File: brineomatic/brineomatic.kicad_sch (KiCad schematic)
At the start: 9 parts, among them J21 Conn_01x04_MountingPin

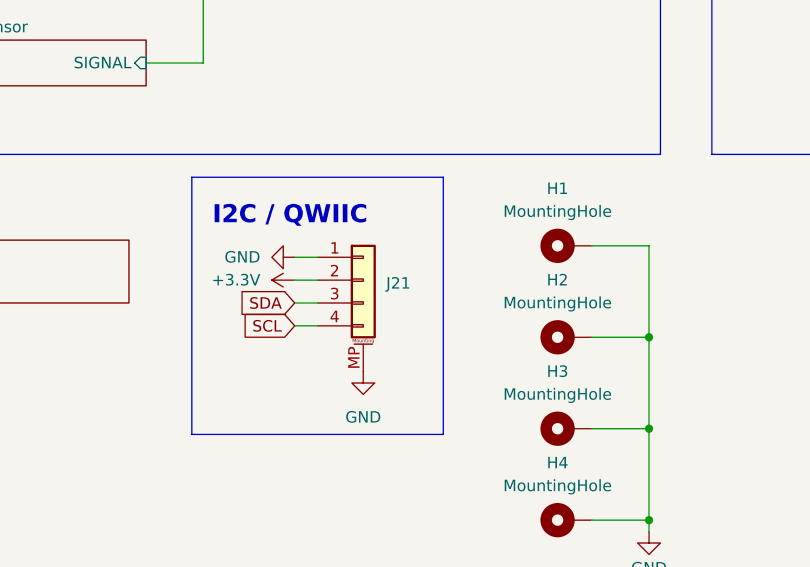
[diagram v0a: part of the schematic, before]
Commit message: added pullup resistor to adc alert
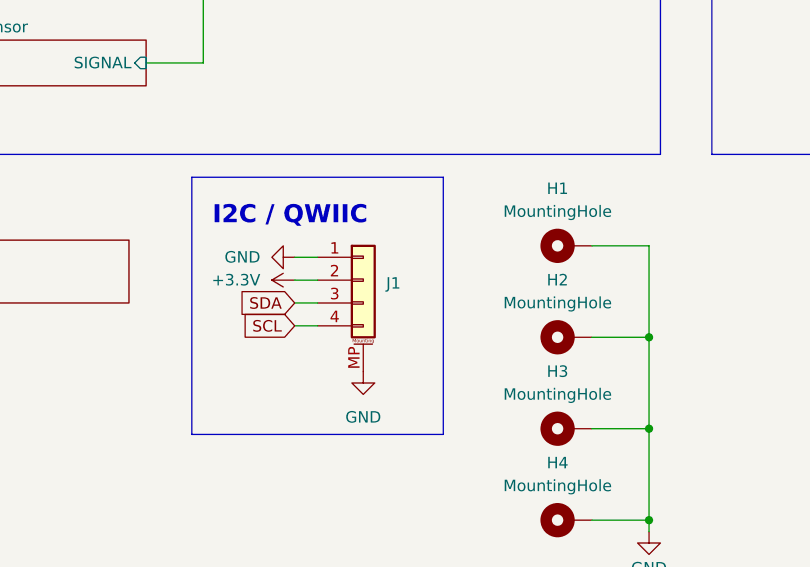
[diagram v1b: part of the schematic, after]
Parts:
- renumbered J21 to J1
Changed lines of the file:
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@@
 		(on_board yes)
 		(dnp no)
-		(property "Reference" "J21"
+		(property "Reference" "J1"
 			(at 92.71 159.1055 0)
 			(effects
@@
 			(project ""
 				(path "/96477ae2-ef08-48f3-8dd4-fe4478541f68"
-					(reference "J21")
+					(reference "J1")
 					(unit 1)
 				)
@@
 		(dnp no)
 		(fields_autoplaced yes)
-		(property "Reference" "#PWR047"
+		(property "Reference" "#PWR03"
 			(at 86.36 158.75 0)
 			(effects
@@
 			(project "brineomatic"
 				(path "/96477ae2-ef08-48f3-8dd4-fe4478541f68"
-					(reference "#PWR047")
+					(reference "#PWR03")
 					(unit 1)
 				)
@@
 		(dnp no)
 		(fields_autoplaced yes)
-		(property "Reference" "#PWR02"
+		(property "Reference" "#PWR01"
 			(at 50.8 63.5 0)
 			(effects
@@
 			(project "brineomatic"
 				(path "/96477ae2-ef08-48f3-8dd4-fe4478541f68"
-					(reference "#PWR02")
+					(reference "#PWR01")
 					(unit 1)
 				)
@@
 		(dnp no)
 		(fields_autoplaced yes)
-		(property "Reference" "#PWR05"
+		(property "Reference" "#PWR07"
 			(at 242.57 95.25 0)
 			(effects
@@
 			(project "brineomatic"
 				(path "/96477ae2-ef08-48f3-8dd4-fe4478541f68"
-					(reference "#PWR05")
+					(reference "#PWR07")
 					(unit 1)
 				)
@@
 		(dnp no)
 		(fields_autoplaced yes)
-		(property "Reference" "#PWR06"
+		(property "Reference" "#PWR08"
 			(at 248.92 73.66 0)
 			(effects
@@
 			(project "brineomatic"
 				(path "/96477ae2-ef08-48f3-8dd4-fe4478541f68"
-					(reference "#PWR06")
+					(reference "#PWR08")
 					(unit 1)
 				)
@@
 		(on_board yes)
 		(dnp no)
-		(property "Reference" "#PWR01"
+		(property "Reference" "#PWR06"
 			(at 121.92 193.04 0)
 			(effects
@@
 			(project "brineomatic"
 				(path "/96477ae2-ef08-48f3-8dd4-fe4478541f68"
-					(reference "#PWR01")
+					(reference "#PWR06")
 					(unit 1)
 				)
@@
 		(dnp no)
 		(fields_autoplaced yes)
-		(property "Reference" "#PWR048"
+		(property "Reference" "#PWR04"
 			(at 90.17 175.26 0)
 			(effects
@@
 			(project "brineomatic"
 				(path "/96477ae2-ef08-48f3-8dd4-fe4478541f68"
-					(reference "#PWR048")
+					(reference "#PWR04")
 					(unit 1)
 				)
@@
 		(dnp no)
 		(fields_autoplaced yes)
-		(property "Reference" "#PWR03"
+		(property "Reference" "#PWR05"
 			(at 104.14 113.03 0)
 			(effects
@@
 			(project ""
 				(path "/96477ae2-ef08-48f3-8dd4-fe4478541f68"
-					(reference "#PWR03")
+					(reference "#PWR05")
 					(unit 1)
 				)
@@
 		(dnp no)
 		(fields_autoplaced yes)
-		(property "Reference" "#PWR04"
+		(property "Reference" "#PWR02"
 			(at 76.2 156.21 0)
 			(effects
@@
 			(project "brineomatic"
 				(path "/96477ae2-ef08-48f3-8dd4-fe4478541f68"
-					(reference "#PWR04")
-					(unit 1)
-				)
+					(reference "#PWR02")
+					(unit 1)
+				)

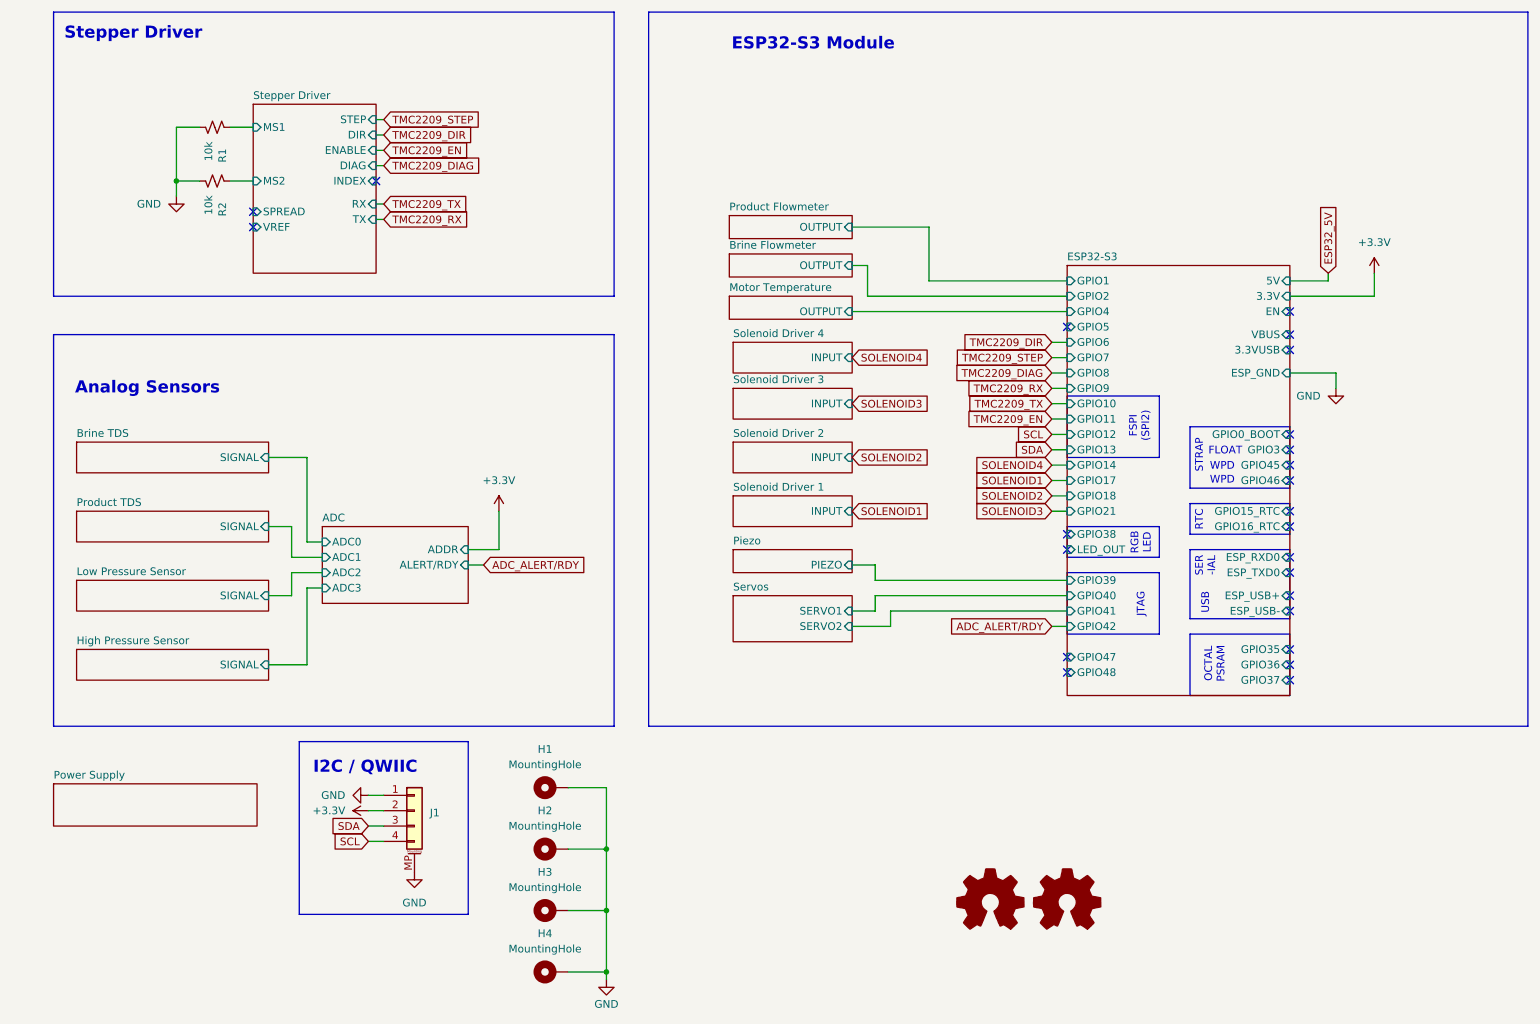
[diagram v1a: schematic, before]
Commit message: added rs485 circuit
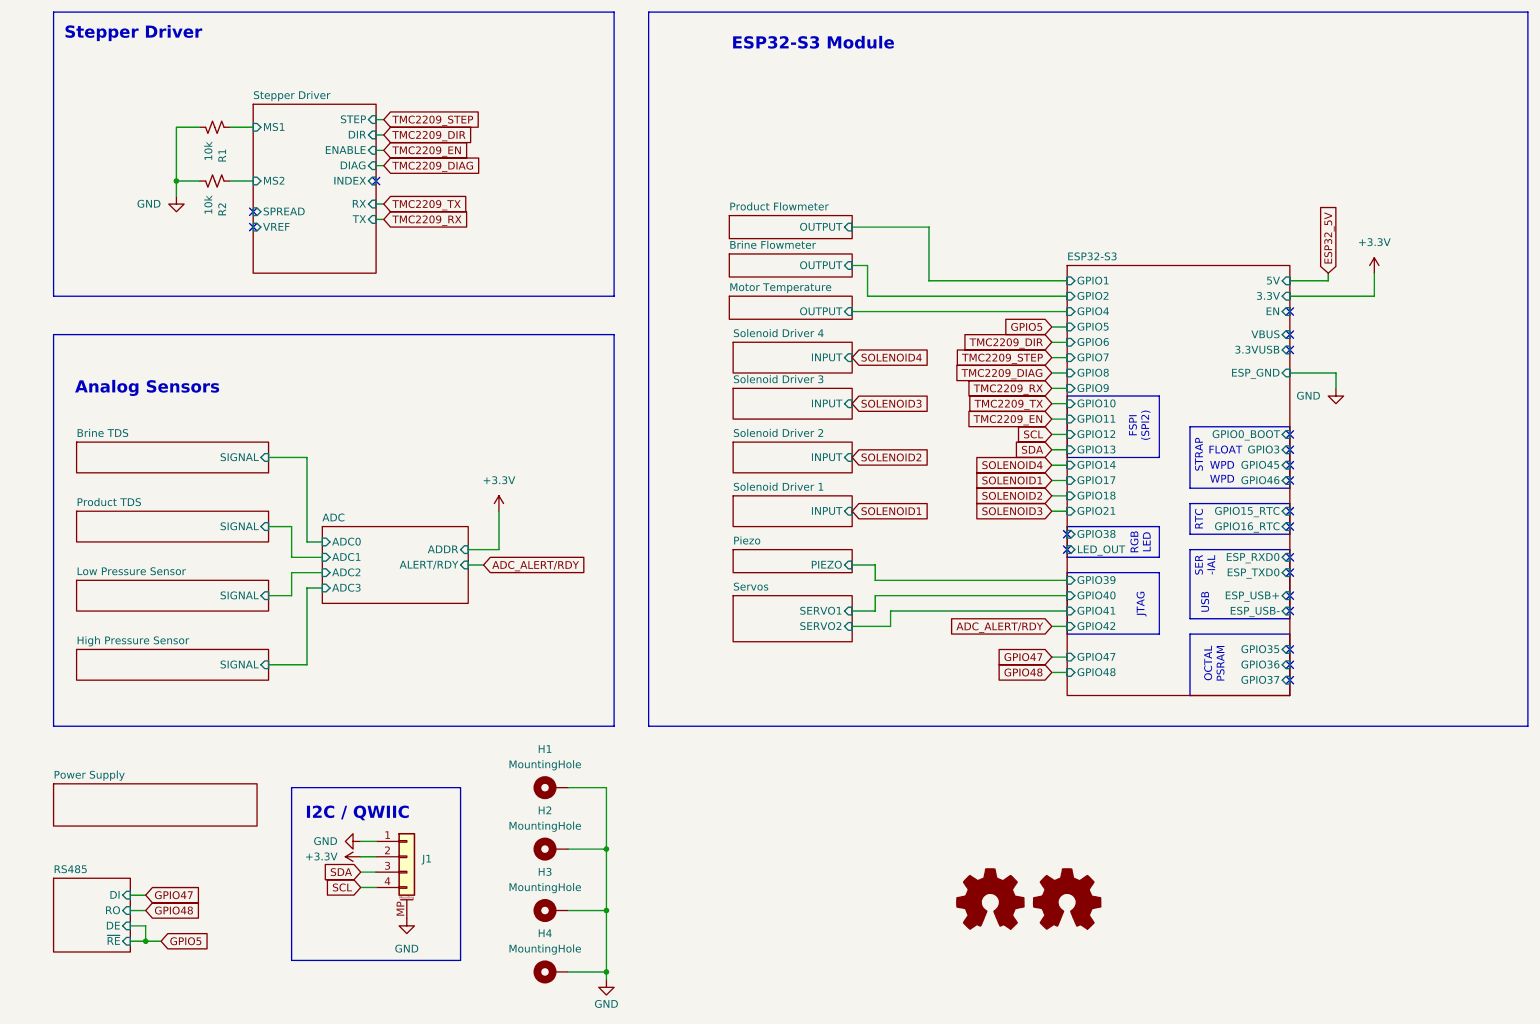
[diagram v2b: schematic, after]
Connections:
- no-connect marks 24 -> 21
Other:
- added sheet RS485 (rs485.kicad_sch)
- moved on the sheet: J1

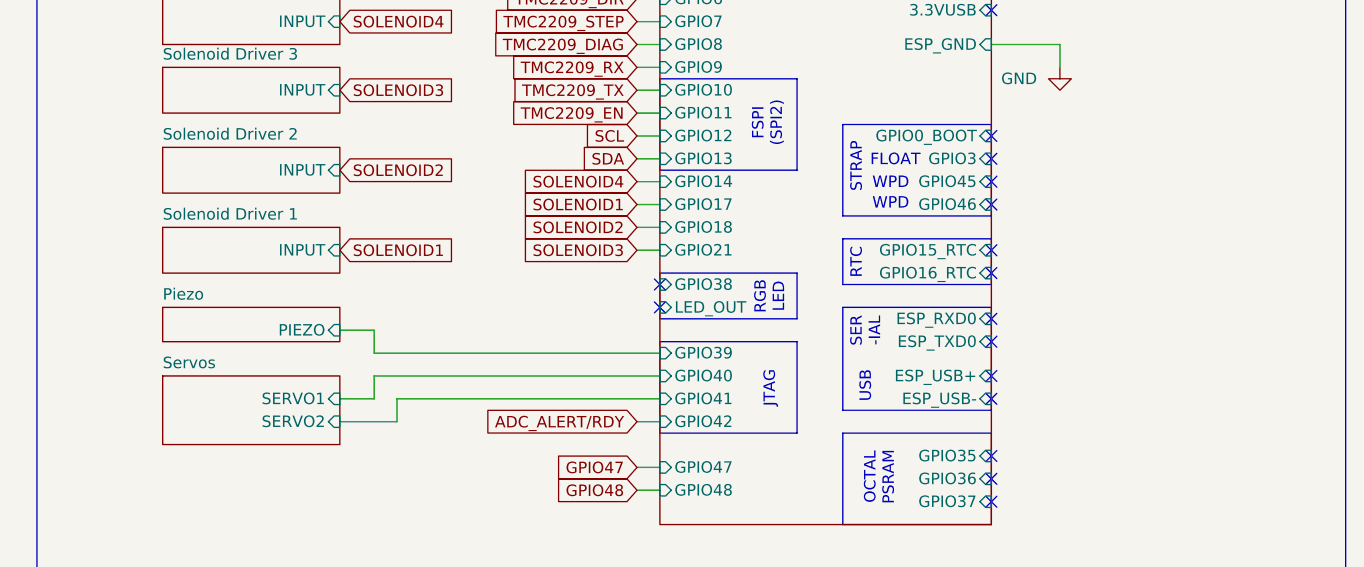
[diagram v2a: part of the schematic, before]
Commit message: added water temperature connector
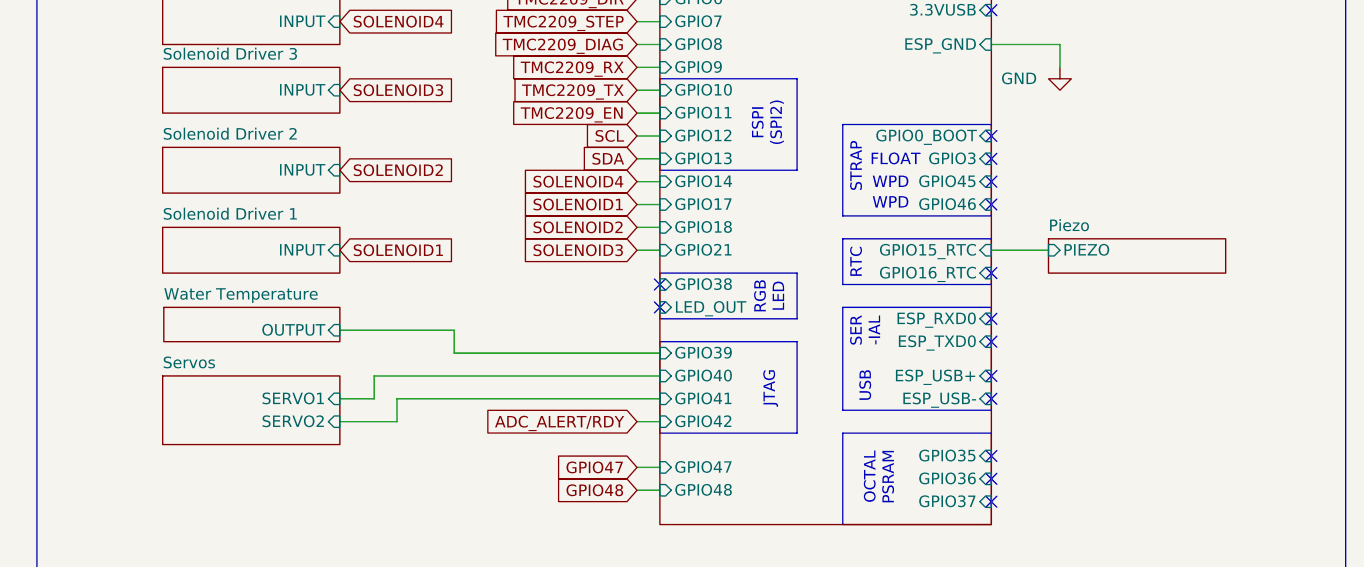
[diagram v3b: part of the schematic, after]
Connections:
- no-connect marks 21 -> 20
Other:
- added sheet Water Temperature (DS18B20.kicad_sch)
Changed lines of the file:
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@@
 	)
 	(no_connect
-		(at 234.95 109.22)
-	)
-	(no_connect
 		(at 234.95 76.2)
 	)
@@
 	(wire
 		(pts
-			(xy 121.92 175.26) (xy 121.92 185.42)
+			(xy 175.26 120.65) (xy 198.12 120.65)
 		)
 		(stroke
@@
 	(wire
 		(pts
-			(xy 166.37 125.73) (xy 166.37 123.19)
+			(xy 121.92 175.26) (xy 121.92 185.42)
 		)
 		(stroke
@@
 	(wire
 		(pts
-			(xy 162.56 118.11) (xy 166.37 118.11)
+			(xy 166.37 125.73) (xy 166.37 123.19)
 		)
 		(stroke
@@
 	(wire
 		(pts
+			(xy 162.56 118.11) (xy 175.26 118.11)
+		)
+		(stroke
+			(width 0)
+			(type default)
+		)
+	)
+	(wire
+		(pts
 			(xy 74.93 114.3) (xy 72.39 114.3)
 		)
@@
 	(wire
 		(pts
+			(xy 234.95 109.22) (xy 241.3 109.22)
+		)
+		(stroke
+			(width 0)
+			(type default)
+		)
+	)
+	(wire
+		(pts
 			(xy 83.82 163.83) (xy 81.28 163.83)
 		)
@@
 	(wire
 		(pts
-			(xy 195.58 86.36) (xy 198.12 86.36)
+			(xy 175.26 118.11) (xy 175.26 120.65)
 		)
 		(stroke
@@
 	(wire
 		(pts
-			(xy 234.95 71.12) (xy 241.3 71.12)
+			(xy 195.58 86.36) (xy 198.12 86.36)
 		)
 		(stroke
@@
 	(wire
 		(pts
-			(xy 175.26 71.12) (xy 198.12 71.12)
+			(xy 234.95 71.12) (xy 241.3 71.12)
 		)
 		(stroke
@@
 	(wire
 		(pts
-			(xy 166.37 120.65) (xy 198.12 120.65)
+			(xy 175.26 71.12) (xy 198.12 71.12)
 		)
 		(stroke
@@
 	(wire
 		(pts
-			(xy 166.37 118.11) (xy 166.37 120.65)
-		)
-		(stroke
-			(width 0)
-			(type default)
-		)
-	)
-	(wire
-		(pts
 			(xy 195.58 128.27) (xy 198.12 128.27)
 		)
@@
 	)
 	(sheet
+		(at 143.002 115.57)
+		(size 19.558 3.81)
+		(exclude_from_sim no)
+		(in_bom yes)
+		(on_board yes)
+		(dnp no)
+		(fields_autoplaced yes)
+		(stroke
+			(width 0.1524)
+			(type solid)
+		)
+		(fill
+			(color 0 0 0 0.0000)
+		)
+		(property "Sheetname" "Water Temperature"
+			(at 143.002 114.8584 0)
+			(effects
+				(font
+					(size 1.27 1.27)
+				)
+				(justify left bottom)
+			)
+		)
+		(property "Sheetfile" "DS18B20.kicad_sch"
+			(at 143.002 119.9646 0)
+			(effects
+				(font
+					(size 1.27 1.27)
+				)
+				(justify left top)
+				(hide yes)
+			)
+		)
+		(pin "OUTPUT" input
+			(at 162.56 118.11 0)
+			(effects
+				(font
+					(size 1.27 1.27)
+				)
+				(justify right)
+			)
+		)
+		(instances
+			(project "brineomatic"
+				(path "/96477ae2-ef08-48f3-8dd4-fe4478541f68"
+					(page "18")
+				)
+			)
+		)
+	)
+	(sheet
 		(at 34.29 109.22)
 		(size 31.75 5.08)
@@
 	)
 	(sheet
-		(at 142.875 115.57)
+		(at 241.3 107.95)
 		(size 19.685 3.81)
 		(exclude_from_sim no)
@@
 		)
 		(property "Sheetname" "Piezo"
-			(at 142.875 114.8584 0)
+			(at 241.3 107.2384 0)
 			(effects
 				(font
@@
 		)
 		(property "Sheetfile" "piezo.kicad_sch"
-			(at 142.875 119.9646 0)
+			(at 241.3 112.3446 0)
 			(effects
 				(font
@@
 		)
 		(pin "PIEZO" input
-			(at 162.56 118.11 0)
+			(at 241.3 109.22 180)
 			(effects
 				(font
 					(size 1.27 1.27)
 				)
-				(justify right)
+				(justify left)
 			)
 		)
